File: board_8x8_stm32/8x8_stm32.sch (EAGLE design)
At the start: 96 parts, among them IC1 STM32F0, J1 SWD_SHROUD, Q1 BSS123, Q10 BSS84, Q11 BSS84, Q12 BSS84, Q13 BSS84, Q14 BSS84, Q15 BSS84, Q16 BSS84, Q2 BSS123, Q3 BSS123, Q4 BSS123, Q5 BSS123, Q6 BSS123, Q7 BSS123, Q8 BSS123, Q9 BSS84

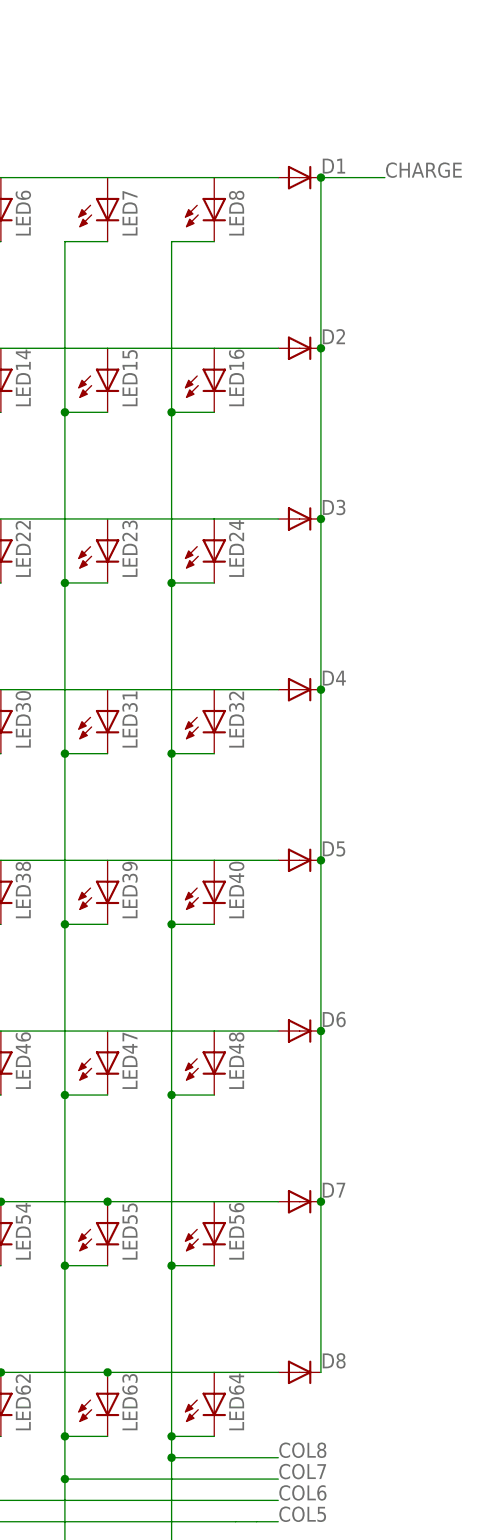
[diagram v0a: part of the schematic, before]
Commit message: adding led photodide sim
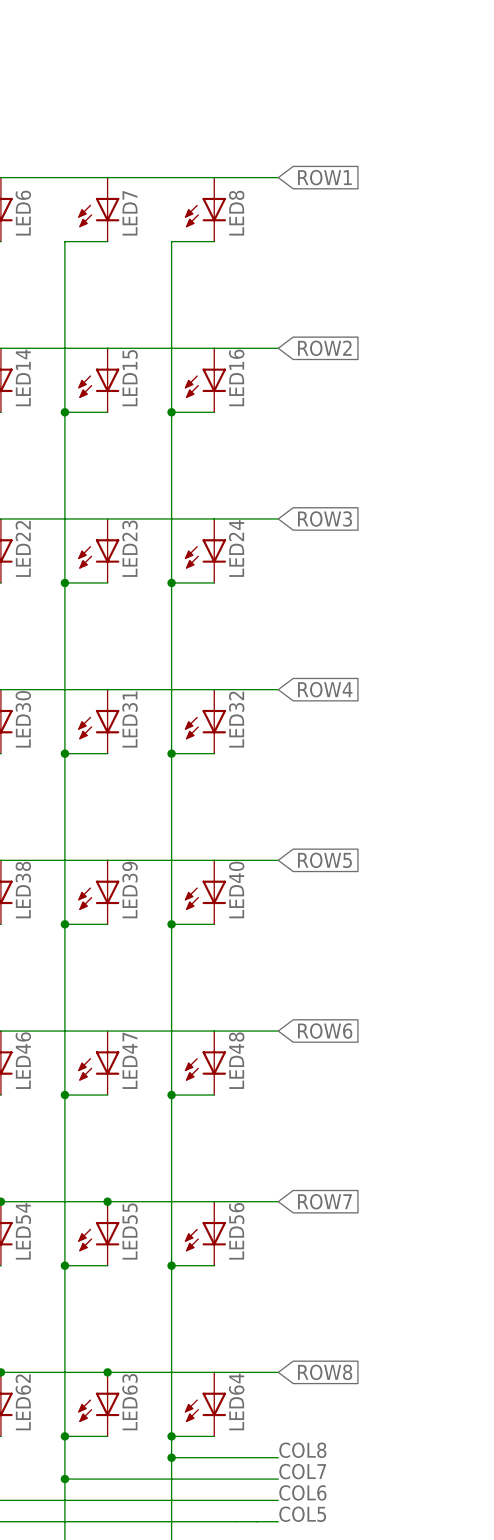
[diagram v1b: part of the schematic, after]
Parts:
- removed D1, D2, D3, D4, D5, D6, D7, D8: (no value), dtb:DIODE-SOD123
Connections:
- removed net CHARGE: D1.C, D2.C, D3.C, D4.C, D5.C, D6.C, D7.C, D8.C
- net ROW1: no longer D1.A
- net ROW2: no longer D2.A
- net ROW3: no longer D3.A
- net ROW4: no longer D4.A
- net ROW5: no longer D5.A
- net ROW6: no longer D6.A
- net ROW7: no longer D7.A
- net ROW8: no longer D8.A
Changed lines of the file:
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@@
 <part name="Q15" library="transistor-small-signal" deviceset="BSS84" device=""/>
 <part name="Q16" library="transistor-small-signal" deviceset="BSS84" device=""/>
-<part name="D1" library="dtb" deviceset="DIODE-" device="SOD123"/>
-<part name="D2" library="dtb" deviceset="DIODE-" device="SOD123"/>
-<part name="D3" library="dtb" deviceset="DIODE-" device="SOD123"/>
-<part name="D4" library="dtb" deviceset="DIODE-" device="SOD123"/>
-<part name="D5" library="dtb" deviceset="DIODE-" device="SOD123"/>
-<part name="D6" library="dtb" deviceset="DIODE-" device="SOD123"/>
-<part name="D7" library="dtb" deviceset="DIODE-" device="SOD123"/>
-<part name="D8" library="dtb" deviceset="DIODE-" device="SOD123"/>
 <part name="J1" library="dtb" deviceset="SWD_SHROUD" device=""/>
 <part name="SV1" library="con-lstb" deviceset="MA03-2" device=""/>
@@
 <instance part="Q15" gate="G$1" x="142.24" y="35.56" rot="R90"/>
 <instance part="Q16" gate="G$1" x="142.24" y="55.88" rot="R90"/>
-<instance part="D1" gate="G$1" x="256.54" y="116.84"/>
-<instance part="D2" gate="G$1" x="256.54" y="96.52"/>
-<instance part="D3" gate="G$1" x="256.54" y="76.2"/>
-<instance part="D4" gate="G$1" x="256.54" y="55.88"/>
-<instance part="D5" gate="G$1" x="256.54" y="35.56"/>
-<instance part="D6" gate="G$1" x="256.54" y="15.24"/>
-<instance part="D7" gate="G$1" x="256.54" y="-5.08"/>
-<instance part="D8" gate="G$1" x="256.54" y="-25.4"/>
 <instance part="J1" gate="G$1" x="33.02" y="139.7"/>
 <instance part="SV1" gate="1" x="-2.54" y="-33.02"/>
@@
 <wire x1="147.32" y1="116.84" x2="246.38" y2="116.84" width="0.1524" layer="91"/>
 <pinref part="Q9" gate="G$1" pin="D"/>
-<pinref part="D1" gate="G$1" pin="A"/>
 <wire x1="254" y1="116.84" x2="246.38" y2="116.84" width="0.1524" layer="91"/>
+<label x="254" y="116.84" size="1.778" layer="95" xref="yes"/>
 </segment>
 </net>
@@
 <wire x1="147.32" y1="96.52" x2="233.68" y2="96.52" width="0.1524" layer="91"/>
 <pinref part="Q10" gate="G$1" pin="D"/>
-<pinref part="D2" gate="G$1" pin="A"/>
 <wire x1="254" y1="96.52" x2="246.38" y2="96.52" width="0.1524" layer="91"/>
+<label x="254" y="96.52" size="1.778" layer="95" xref="yes"/>
 </segment>
 </net>
@@
 <wire x1="246.38" y1="76.2" x2="147.32" y2="76.2" width="0.1524" layer="91"/>
 <pinref part="Q11" gate="G$1" pin="D"/>
-<pinref part="D3" gate="G$1" pin="A"/>
 <wire x1="254" y1="76.2" x2="246.38" y2="76.2" width="0.1524" layer="91"/>
+<label x="254" y="76.2" size="1.778" layer="95" xref="yes"/>
 </segment>
 </net>
@@
 <wire x1="246.38" y1="55.88" x2="147.32" y2="55.88" width="0.1524" layer="91"/>
 <pinref part="Q16" gate="G$1" pin="D"/>
-<pinref part="D4" gate="G$1" pin="A"/>
 <wire x1="254" y1="55.88" x2="246.38" y2="55.88" width="0.1524" layer="91"/>
+<label x="254" y="55.88" size="1.778" layer="95" xref="yes"/>
 </segment>
 </net>
@@
 <wire x1="246.38" y1="35.56" x2="147.32" y2="35.56" width="0.1524" layer="91"/>
 <pinref part="Q15" gate="G$1" pin="D"/>
-<pinref part="D5" gate="G$1" pin="A"/>
 <wire x1="254" y1="35.56" x2="246.38" y2="35.56" width="0.1524" layer="91"/>
+<label x="254" y="35.56" size="1.778" layer="95" xref="yes"/>
 </segment>
 </net>
@@
 <wire x1="246.38" y1="15.24" x2="147.32" y2="15.24" width="0.1524" layer="91"/>
 <pinref part="Q14" gate="G$1" pin="D"/>
-<pinref part="D6" gate="G$1" pin="A"/>
 <wire x1="254" y1="15.24" x2="246.38" y2="15.24" width="0.1524" layer="91"/>
+<label x="254" y="15.24" size="1.778" layer="95" xref="yes"/>
 </segment>
 </net>
@@
 <junction x="233.68" y="-5.08"/>
 <pinref part="Q13" gate="G$1" pin="D"/>
-<pinref part="D7" gate="G$1" pin="A"/>
 <wire x1="254" y1="-5.08" x2="246.38" y2="-5.08" width="0.1524" layer="91"/>
+<label x="254" y="-5.08" size="1.778" layer="95" xref="yes"/>
 </segment>
 </net>
@@
 <wire x1="157.48" y1="-25.4" x2="147.32" y2="-25.4" width="0.1524" layer="91"/>
 <pinref part="Q12" gate="G$1" pin="D"/>
-<pinref part="D8" gate="G$1" pin="A"/>
 <wire x1="254" y1="-25.4" x2="246.38" y2="-25.4" width="0.1524" layer="91"/>
+<label x="254" y="-25.4" size="1.778" layer="95" xref="yes"/>
 </segment>
 </net>
@@
 </segment>
 </net>
-<net name="CHARGE" class="0">
-<segment>
-<pinref part="D1" gate="G$1" pin="C"/>
-<wire x1="266.7" y1="116.84" x2="259.08" y2="116.84" width="0.1524" layer="91"/>
-<pinref part="D8" gate="G$1" pin="C"/>
-<wire x1="259.08" y1="116.84" x2="259.08" y2="96.52" width="0.1524" layer="91"/>
-<pinref part="D7" gate="G$1" pin="C"/>
-<junction x="259.08" y="-5.08"/>
-<wire x1="259.08" y1="96.52" x2="259.08" y2="76.2" width="0.1524" layer="91"/>
-<wire x1="259.08" y1="76.2" x2="259.08" y2="55.88" width="0.1524" layer="91"/>
-<wire x1="259.08" y1="55.88" x2="259.08" y2="35.56" width="0.1524" layer="91"/>
-<wire x1="259.08" y1="35.56" x2="259.08" y2="15.24" width="0.1524" layer="91"/>
-<wire x1="259.08" y1="15.24" x2="259.08" y2="-5.08" width="0.1524" layer="91"/>
-<wire x1="259.08" y1="-5.08" x2="259.08" y2="-25.4" width="0.1524" layer="91"/>
-<pinref part="D6" gate="G$1" pin="C"/>
-<junction x="259.08" y="15.24"/>
-<pinref part="D5" gate="G$1" pin="C"/>
-<junction x="259.08" y="35.56"/>
-<pinref part="D4" gate="G$1" pin="C"/>
-<junction x="259.08" y="55.88"/>
-<pinref part="D3" gate="G$1" pin="C"/>
-<junction x="259.08" y="76.2"/>
-<pinref part="D2" gate="G$1" pin="C"/>
-<junction x="259.08" y="96.52"/>
-<junction x="259.08" y="116.84"/>
-<label x="266.7" y="116.84" size="1.778" layer="95"/>
-</segment>
-</net>

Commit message: playing about with different deisgns
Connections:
- removed net SHIFT_CLK: SV2.2, SV4.2
- new net N$9: Q10.S, Q11.S, Q12.S, Q13.S, Q14.S, Q15.S, Q16.S, Q9.S
- new net SHIFT_LEFT: SV4.5
- new net SHIFT_RIGHT: SV2.5
- net CFET1: now also IC1.PB0
- net CFET2: now also IC1.PB1
- net CFET3: now also IC1.PB2
- net CFET4: now also IC1.PB3
- net CFET5: now also IC1.PB4
- net CFET6: now also IC1.PB5
- net CFET7: now also IC1.PB6
- net CFET8: now also IC1.PB7
- net COL1: now also IC1.PB8
- net COL2: now also IC1.PB9
- net COL3: now also IC1.PB10
- net COL4: now also IC1.PB11
- net COL5: now also IC1.PB12
- net COL6: now also IC1.PB13
- net COL7: now also IC1.PB14
- net COL8: now also IC1.PB15
- net ROW1: now also LED1.A, LED2.A, LED3.A, LED4.A, LED5.A, LED6.A, LED7.A
- net ROW2: now also LED10.A, LED11.A, LED12.A, LED13.A, LED14.A, LED9.A
- net ROW3: now also LED17.A, LED18.A, LED19.A, LED20.A, LED21.A, LED22.A, LED23.A
- net ROW4: now also LED25.A, LED26.A, LED27.A, LED28.A, LED29.A, LED30.A, LED31.A
- net ROW5: now also LED33.A, LED34.A, LED35.A, LED36.A, LED37.A, LED38.A, LED39.A
- net ROW6: now also LED41.A, LED42.A, LED43.A, LED44.A, LED45.A, LED46.A, LED47.A

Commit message: adding a couple of notes
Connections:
- removed net N$9: Q10.S, Q11.S, Q12.S, Q13.S, Q14.S, Q15.S, Q16.S, Q9.S
- new net +5V: Q10.S, Q11.S, Q12.S, Q13.S, Q14.S, Q15.S, Q16.S, Q9.S, SV2.6, SV4.6
- new net N$10: IC1.PA9
- net +3V3: now also SV2.2, SV4.2
- net G_UART: now also IC1.PA10
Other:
- note added: "ftdi"
- note added: "this pins need 5V tolerant pins, which is all IO except pins 10-19"
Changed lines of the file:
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@@
 <part name="+3V2" library="supply1" deviceset="+3V3" device=""/>
 <part name="+3V3" library="supply1" deviceset="+3V3" device=""/>
+<part name="P+1" library="supply1" deviceset="+5V" device=""/>
+<part name="P+2" library="supply1" deviceset="+5V" device=""/>
+<part name="P+3" library="supply1" deviceset="+5V" device=""/>
+<part name="+3V4" library="supply1" deviceset="+3V3" device=""/>
+<part name="+3V5" library="supply1" deviceset="+3V3" device=""/>
 </parts>
 <sheets>
 <sheet>
 <plain>
+<text x="129.54" y="53.34" size="1.778" layer="91" rot="R90">this pins need 5V tolerant pins, which is all IO except pins 10-19</text>
+<text x="271.78" y="48.26" size="1.778" layer="91" rot="R90">this pins need 5V tolerant pins, which is all IO except pins 10-19</text>
+<text x="66.04" y="129.54" size="1.778" layer="91">ftdi</text>
 </plain>
 <instances>
@@
 <instance part="+3V2" gate="G$1" x="0" y="83.82"/>
 <instance part="+3V3" gate="G$1" x="15.24" y="149.86"/>
+<instance part="P+1" gate="1" x="134.62" y="129.54"/>
+<instance part="P+2" gate="1" x="-43.18" y="-50.8"/>
+<instance part="P+3" gate="1" x="22.86" y="-53.34"/>
+<instance part="+3V4" gate="G$1" x="-43.18" y="-60.96" rot="R90"/>
+<instance part="+3V5" gate="G$1" x="22.86" y="-63.5" rot="R90"/>
 </instances>
 <busses>
@@
 <label x="17.78" y="-60.96" size="1.778" layer="95" rot="MR0"/>
 </segment>
+<segment>
+<pinref part="IC1" gate="G$1" pin="PA10"/>
+<wire x1="63.5" y1="93.98" x2="68.58" y2="93.98" width="0.1524" layer="91"/>
+<label x="68.58" y="93.98" size="1.778" layer="95"/>
+<wire x1="68.58" y1="93.98" x2="76.2" y2="93.98" width="0.1524" layer="91"/>
+<wire x1="68.58" y1="93.98" x2="68.58" y2="129.54" width="0.1524" layer="91"/>
+<junction x="68.58" y="93.98"/>
+</segment>
 </net>
 <net name="NRST" class="0">
@@
 <wire x1="15.24" y1="144.78" x2="15.24" y2="147.32" width="0.1524" layer="91"/>
 </segment>
+<segment>
+<pinref part="SV4" gate="1" pin="2"/>
+<pinref part="+3V4" gate="G$1" pin="+3V3"/>
+</segment>
+<segment>
+<pinref part="SV2" gate="1" pin="2"/>
+<pinref part="+3V5" gate="G$1" pin="+3V3"/>
+</segment>
 </net>
 <net name="SHIFT_LEFT" class="0">
@@
 </segment>
 </net>
-<net name="N$9" class="0">
+<net name="N$10" class="0">
+<segment>
+<pinref part="IC1" gate="G$1" pin="PA9"/>
+<wire x1="63.5" y1="96.52" x2="66.04" y2="96.52" width="0.1524" layer="91"/>
+<wire x1="66.04" y1="96.52" x2="76.2" y2="96.52" width="0.1524" layer="91"/>
+<wire x1="66.04" y1="96.52" x2="66.04" y2="129.54" width="0.1524" layer="91"/>
+<junction x="66.04" y="96.52"/>
+</segment>
+</net>
+<net name="+5V" class="0">
 <segment>
 <pinref part="Q12" gate="G$1" pin="S"/>
@@
 <junction x="134.62" y="96.52"/>
 <junction x="134.62" y="116.84"/>
-</segment>
-</net>
+<pinref part="P+1" gate="1" pin="+5V"/>
+</segment>
+<segment>
+<pinref part="SV4" gate="1" pin="6"/>
+<pinref part="P+2" gate="1" pin="+5V"/>
+<wire x1="-43.18" y1="-53.34" x2="-40.64" y2="-55.88" width="0.1524" layer="91"/>
+</segment>
+<segment>
+<pinref part="SV2" gate="1" pin="6"/>
+<pinref part="P+3" gate="1" pin="+5V"/>
+<wire x1="22.86" y1="-55.88" x2="25.4" y2="-58.42" width="0.1524" layer="91"/>
+</segment>
+</net>

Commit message: 'done' schematic
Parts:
- added C1, C2, C3, C4, C5, C6, C7, C8: 100p, passives-7351:CAPACITOR0603-N
- added C10, C11, C16, C9: (no value), passives-7351:CAPACITOR0603-N
- added C12, C13: (no value), rcl:CPOL-EUE2-4
- added C14, C15: (no value), rcl:C-EU050-025X075
- added JP1: (no value), Mine:M02PTH
- added JP2: (no value), SparkFun-Connectors:M06SILK_FEMALE_PTH
- added JP3, JP4, JP5, JP6: (no value), SparkFun-Connectors:M08
- added LED65: (no value), dtb:LED5MM
- added LED66: (no value), dtb:LED10MM
- added R1, R2, R3, R4, R5, R6, R7, R8: DNP, passives-7351:RESISTOR0603-N
- added R10: 2k2, passives-7351:RESISTOR0603-N
- added R9: (no value), passives-7351:RESISTOR0603-N
- added RN3, RN4: (no value), resistor-dil:4R-NEXB38V
- added SJ1, SJ2: JUMPER-PAD-2-NC_BY_TRACE, SparkFun-Passives:JUMPER-PAD-2-NC_BY_TRACE
- added U$1: MCP1700, dtb:MCP1700
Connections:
- removed net N$10: IC1.PA9
- new net N$11: IC1.PC15, R10.P$2
- new net N$9: IC1.BOOT0, JP1.2, R9.P$1
- net +3V3: now also C10.1, C11.1, C15.1, C16.1, C9.1, JP2.4, JP3.5, JP4.5, JP5.5, JP6.5, R9.P$2, U$1.OUT
- net +5V: now also C12.+, C13.+, C14.1, JP3.1, JP3.8, JP4.1, JP4.8, JP5.1, JP5.8, JP6.1, JP6.8, RN3A.1, RN3B.1, RN3C.1, RN3D.1, RN4A.1, RN4B.1, RN4C.1, RN4D.1, U$1.IN
- net CFET1: now also IC1.PA0; no longer IC1.PB0
- net CFET2: now also IC1.PA1; no longer IC1.PB1
- net CFET3: now also IC1.PA2; no longer IC1.PB2
- net CFET4: now also IC1.PA3; no longer IC1.PB3
- net CFET5: now also IC1.PA4; no longer IC1.PB4
- net CFET6: now also IC1.PA5; no longer IC1.PB5
- net CFET7: now also IC1.PA6; no longer IC1.PB6
- net CFET8: now also IC1.PA7; no longer IC1.PB7
- net COL1: now also C1.1, R1.P$2, RN1D.2; no longer RN1A.2
- net COL2: now also C2.1, R2.P$2, RN1C.2; no longer RN1B.2
- net COL3: now also C3.1, R3.P$2, RN1B.2; no longer RN1C.2
- net COL4: now also C4.1, R4.P$2, RN1A.2; no longer RN1D.2
- net COL5: now also C5.1, R5.P$2
- net COL6: now also C6.1, R6.P$2
- net COL7: now also C7.1, R7.P$2
- net COL8: now also C8.1, R10.P$1, R8.P$2; no longer IC1.PB15
- net COMMS_DOWN: now also IC1.PB1, JP5.3
- net COMMS_LEFT: now also IC1.PC14, JP4.3
- net COMMS_RIGHT: now also IC1.PC13, JP3.3
- net COMMS_UP: now also IC1.PB0, JP6.3
- net GND: now also C1.2, C10.2, C11.2, C12.-, C13.-, C14.2, C15.2, C16.2, C2.2, C3.2, C4.2, C5.2, C6.2, C7.2, C8.2, C9.2, JP1.1, JP2.6, JP3.2, JP3.7, JP4.2, JP4.7, JP5.2, JP5.7, JP6.2, JP6.7, R1.P$1, R2.P$1, R3.P$1, R4.P$1, R5.P$1, R6.P$1, R7.P$1, R8.P$1, U$1.GND
- net G_UART: now also JP2.3, JP3.6, JP4.6, JP5.6, JP6.6
- net N$5: now also RN1A.1; no longer RN1D.1
- net N$6: now also RN1B.1; no longer RN1C.1
- net N$7: now also RN1C.1; no longer RN1B.1
- net N$8: now also RN1D.1; no longer RN1A.1
- net RFET1: now also IC1.PA8, RN4B.2
- net RFET2: now also IC1.PA9, JP2.2, RN4C.2
- net RFET3: now also IC1.PB15, RN4A.2
- net RFET4: now also IC1.PA11, RN4D.2
- net RFET5: now also IC1.PA12, RN3D.2
- net RFET6: now also RN3C.2, SJ1.2
- net RFET7: now also RN3B.2, SJ2.2
- net RFET8: now also IC1.PA15, RN3A.2
- net ROW1: now also IC1.PF0
- net ROW2: now also IC1.PF1
- net ROW3: now also IC1.PB2
- net ROW4: now also IC1.PB3
- net ROW5: now also IC1.PB4
- net ROW6: now also IC1.PB5
- net ROW7: now also IC1.PB6
- net ROW8: now also IC1.PB7
- net SHIFT_LEFT: now also IC1.PF7, JP4.4
- net SHIFT_RIGHT: now also IC1.PF6, JP3.4
- net SWCLK: now also SJ2.1
- net SWDAT: now also SJ1.1
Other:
- note added: "< resistor? >"
- note removed: "ftdi"
- moved on the sheet: RN1A, RN1B, RN1C, RN1D

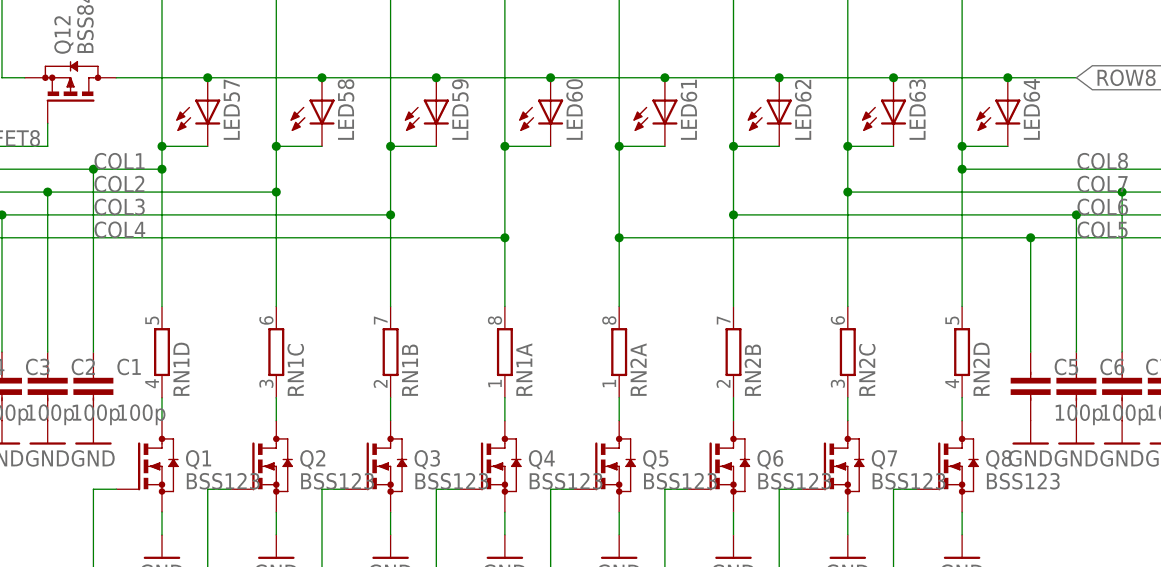
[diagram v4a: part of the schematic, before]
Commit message: chnaging to combined led footprint
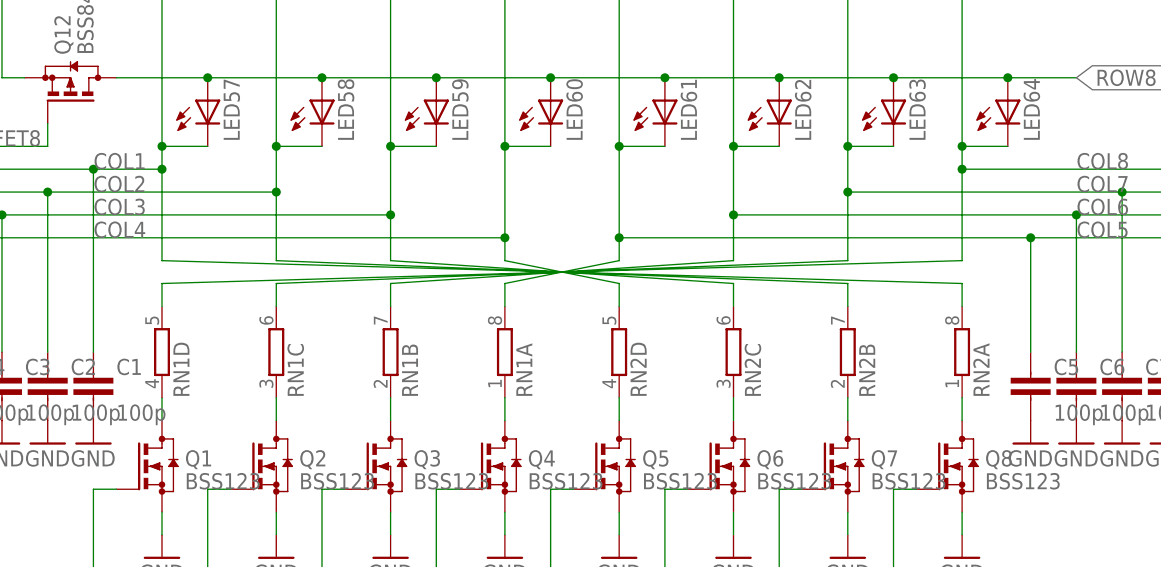
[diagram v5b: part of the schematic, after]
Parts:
- LED1, LED10, LED11, LED12, LED13, LED14, LED15, LED16, LED17, LED18, LED19, LED2, LED20, LED21, LED22, LED23, LED24, LED25, LED26, LED27, LED28, LED29, LED3, LED30, LED31, LED32, LED33, LED34, LED35, LED36, LED37, LED38, LED39, LED4, LED40, LED41, LED42, LED43, LED44, LED45, LED46, LED47, LED48, LED49, LED5, LED50, LED51, LED52, LED53, LED54, LED55, LED56, LED57, LED58, LED59, LED6, LED60, LED61, LED62, LED63, LED64, LED7, LED8, LED9: device dtb:LEDCHIP-LED0603 -> dtb:LED5MM/0603
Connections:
- net COL1: now also RN2A.2; no longer RN1D.2
- net COL2: now also RN2B.2; no longer RN1C.2
- net COL3: now also RN2C.2; no longer RN1B.2
- net COL4: now also RN2D.2; no longer RN1A.2
- net COL5: now also RN1A.2; no longer RN2A.2
- net COL6: now also RN1B.2; no longer RN2B.2
- net COL7: now also RN1C.2; no longer RN2C.2
- net COL8: now also RN1D.2; no longer RN2D.2
- net N$1: now also RN2A.1; no longer RN2D.1
- net N$2: now also RN2B.1; no longer RN2C.1
- net N$3: now also RN2C.1; no longer RN2B.1
- net N$4: now also RN2D.1; no longer RN2A.1
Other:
- moved on the sheet: RN2A, RN2B, RN2C, RN2D

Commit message: routing...
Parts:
- removed LED65: (no value), dtb:LED5MM
- removed LED66: (no value), dtb:LED10MM
- removed SV1, SV2, SV3, SV4: (no value), con-lstb:MA03-2
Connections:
- net +3V3: no longer SV2.2, SV4.2
- net +5V: no longer SV2.6, SV4.6
- net COMMS_DOWN: no longer SV3.3
- net COMMS_LEFT: no longer SV4.3
- net COMMS_RIGHT: no longer SV2.3
- net COMMS_UP: no longer SV1.3
- net GND: no longer SV1.1, SV2.1, SV3.1, SV4.1
- net G_UART: no longer SV1.4, SV2.4, SV3.4, SV4.4
- net RFET1: now also IC1.PA12; no longer IC1.PA8
- net RFET2: now also SJ1.2; no longer IC1.PA9, JP2.2
- net RFET3: now also SJ2.2; no longer IC1.PB15
- net RFET4: now also IC1.PA15; no longer IC1.PA11
- net RFET5: now also IC1.PA8, RN3B.2; no longer IC1.PA12, RN3D.2
- net RFET6: now also IC1.PA9, JP2.2; no longer SJ1.2
- net RFET7: now also IC1.PB15, RN3A.2; no longer RN3B.2, SJ2.2
- net RFET8: now also IC1.PA11, RN3D.2; no longer IC1.PA15, RN3A.2
- net SHIFT_LEFT: no longer SV4.5
- net SHIFT_RIGHT: no longer SV2.5
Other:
- moved on the sheet: RN3A, RN3B, RN3D

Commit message: more routig..
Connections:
- net COL1: now also C6.1, IC1.PB13, R6.P$2; no longer C1.1, IC1.PB8, R1.P$2
- net COL2: now also C5.1, IC1.PB12, R5.P$2; no longer C2.1, IC1.PB9, R2.P$2
- net COL5: now also C7.1, IC1.PB14, R7.P$2; no longer C5.1, IC1.PB12, R5.P$2
- net COL6: now also C2.1, IC1.PB9, R2.P$2; no longer C6.1, IC1.PB13, R6.P$2
- net COL7: now also C1.1, IC1.PB8, R1.P$2; no longer C7.1, IC1.PB14, R7.P$2
- net RFET1: now also RN4D.2; no longer RN4B.2
- net RFET3: now also RN4B.2; no longer RN4A.2
- net RFET4: now also RN4A.2; no longer RN4D.2
- net RFET5: now also RN3D.2; no longer RN3B.2
- net RFET6: now also RN3A.2; no longer RN3C.2
- net RFET7: now also RN3B.2; no longer RN3A.2
- net RFET8: now also RN3C.2; no longer RN3D.2
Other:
- moved on the sheet: C1, C6, C7, R1, R6, R7, RN3A, RN3B, RN3C, RN3D, RN4A, RN4B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
